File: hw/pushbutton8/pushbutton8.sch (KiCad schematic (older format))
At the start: 34 parts, among them U1 74HC595

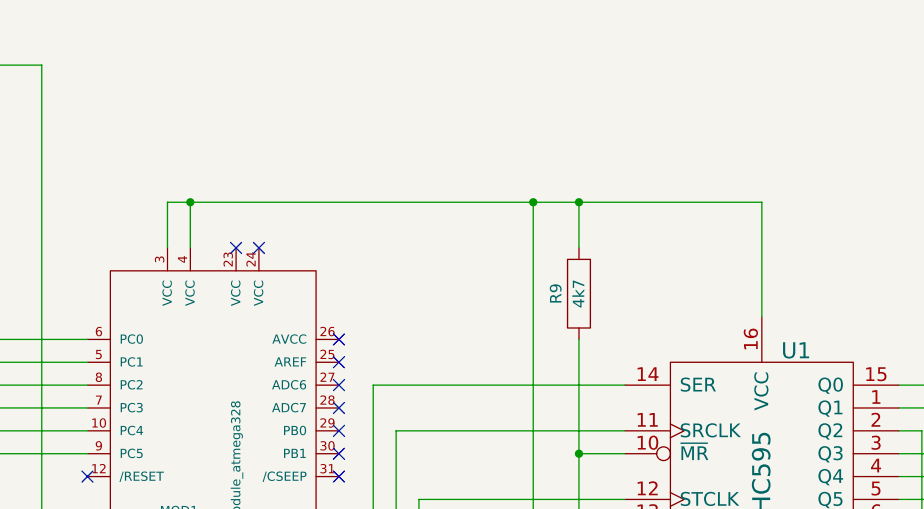
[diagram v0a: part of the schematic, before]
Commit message: Added first iteration of rev B  - usable with Reb B and newer bus-modules which have 24V on header
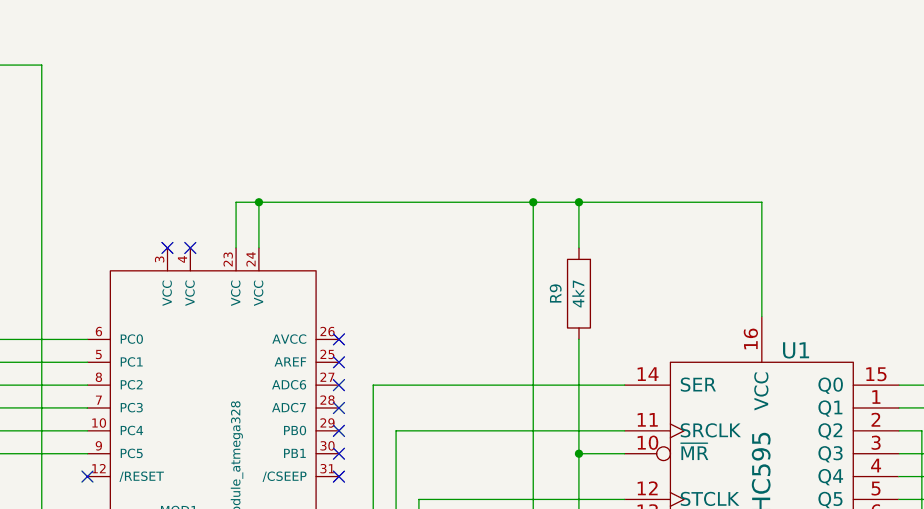
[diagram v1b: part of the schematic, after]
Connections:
- net at MOD1.23 (VCC): now also C1.1, MOD1.24 (VCC), R9.1, U1.16 (VCC)
- now unconnected: MOD1.3 (VCC), MOD1.4 (VCC)
